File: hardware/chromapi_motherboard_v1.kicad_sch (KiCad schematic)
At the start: 9 parts

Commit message: add spi todo
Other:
- note added: "[todo] correct SPI MISO/MOSI connection mismatch"
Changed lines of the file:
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@@
+		)
+	)
+	(text "[todo] correct SPI MISO/MOSI connection mismatch"
+		(exclude_from_sim no)
+		(at 182.118 57.404 0)
+		(effects
+			(font
+				(size 1.27 1.27)
+			)
+			(justify left bottom)
 		)
 	)

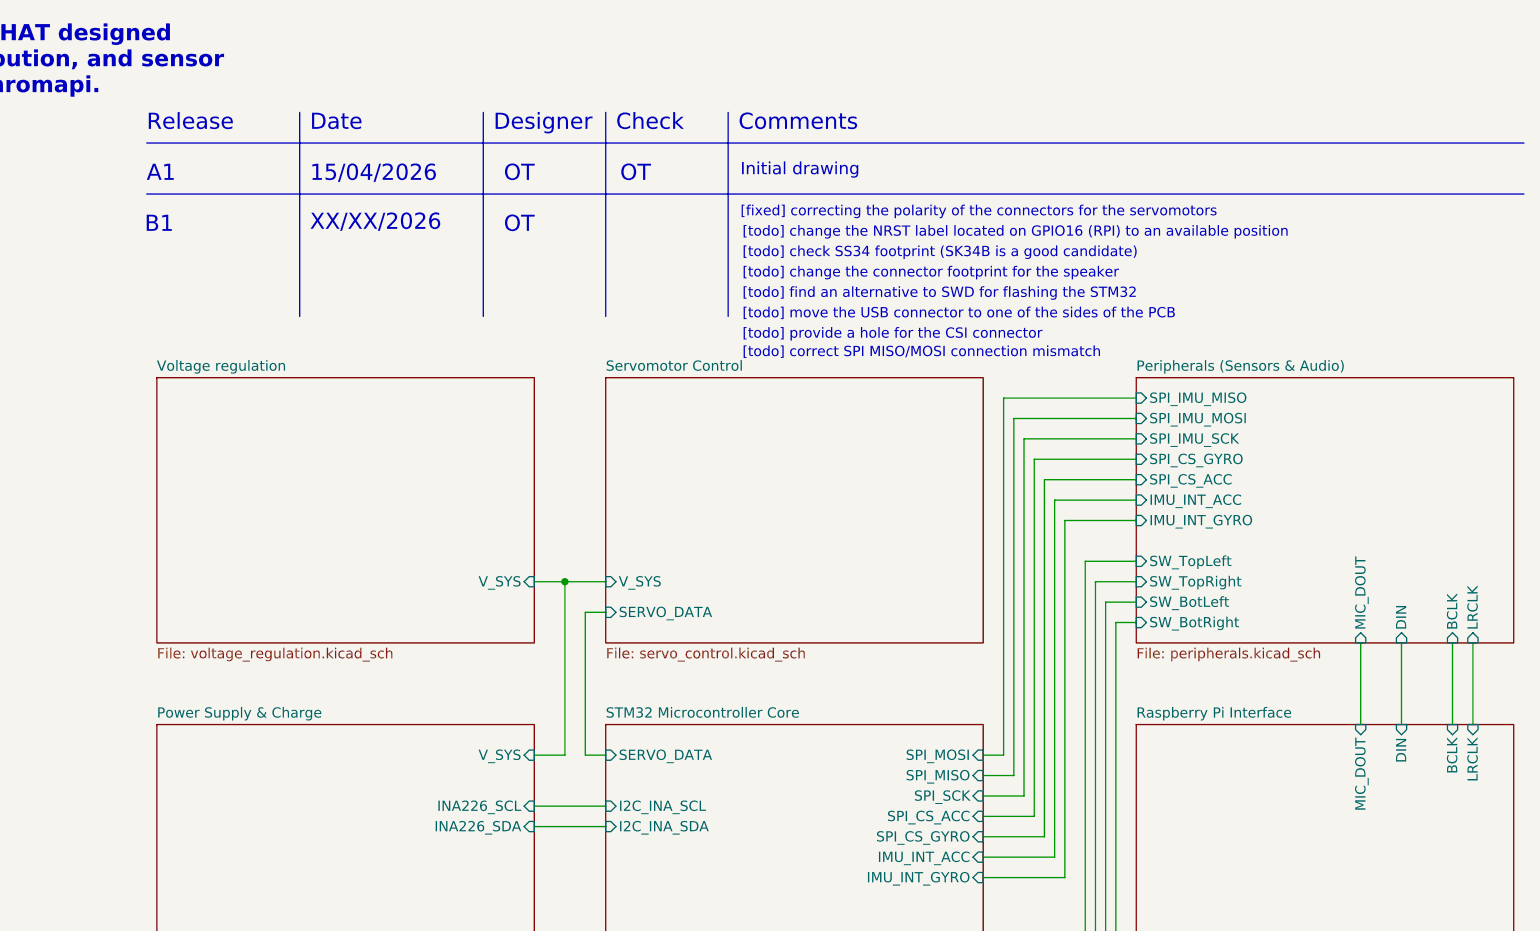
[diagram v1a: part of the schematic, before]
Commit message: fix spi connection mismatch
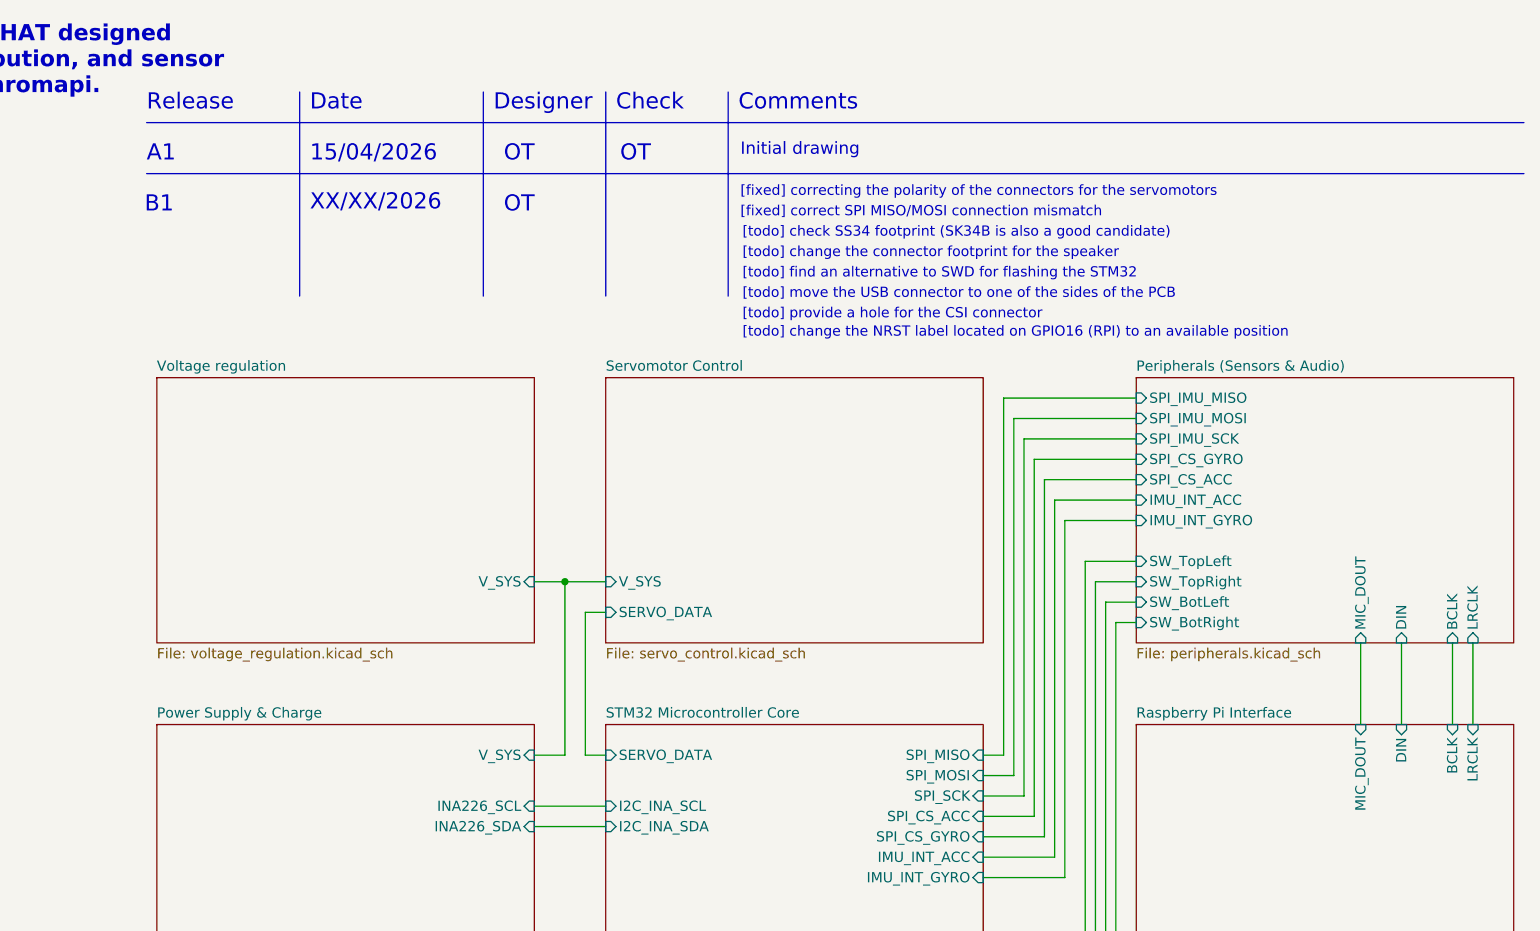
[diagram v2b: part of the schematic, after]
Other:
- note added: "[fixed] correct SPI MISO/MOSI connection mismatch"
- note added: "[todo] check SS34 footprint (SK34B is also a good candidate)"
- note removed: "[todo] check SS34 footprint (SK34B is a good candidate)"
- note removed: "[todo] correct SPI MISO/MOSI connection mismatch"
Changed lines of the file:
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@@
 	(text "[todo] change the connector footprint for the speaker"
 		(exclude_from_sim no)
-		(at 182.118 47.498 0)
+		(at 182.118 44.958 0)
 		(effects
 			(font
@@
 	(text "[todo] change the NRST label located on GPIO16 (RPI) to an available position"
 		(exclude_from_sim no)
-		(at 182.118 42.418 0)
+		(at 182.118 54.864 0)
 		(effects
 			(font
@@
 		)
 	)
-	(text "[todo] check SS34 footprint (SK34B is a good candidate)"
+	(text "[todo] check SS34 footprint (SK34B is also a good candidate)"
 		(exclude_from_sim no)
-		(at 182.118 44.958 0)
+		(at 182.118 42.418 0)
 		(effects
 			(font
@@
 	(text "Check"
 		(exclude_from_sim no)
-		(at 166.37 29.21 0)
+		(at 166.37 26.67 0)
 		(effects
 			(font
@@
 	(text "[fixed] correcting the polarity of the connectors for the servomotors"
 		(exclude_from_sim no)
-		(at 181.864 39.878 0)
+		(at 181.864 37.338 0)
 		(effects
 			(font
@@
 	(text "B1"
 		(exclude_from_sim no)
-		(at 107.696 41.91 0)
+		(at 107.696 39.37 0)
 		(effects
 			(font
@@
 	(text "[todo] provide a hole for the CSI connector "
 		(exclude_from_sim no)
-		(at 182.118 55.118 0)
+		(at 182.118 52.578 0)
 		(effects
 			(font
@@
 	(text "OT"
 		(exclude_from_sim no)
-		(at 166.878 35.56 0)
+		(at 166.878 33.02 0)
 		(effects
 			(font
@@
 	(text "OT"
 		(exclude_from_sim no)
-		(at 152.4 41.91 0)
+		(at 152.4 39.37 0)
 		(effects
 			(font
@@
 	(text "Initial drawing"
 		(exclude_from_sim no)
-		(at 181.864 34.798 0)
+		(at 181.864 32.258 0)
 		(effects
 			(font
@@
 	(text "Release"
 		(exclude_from_sim no)
-		(at 107.95 29.21 0)
+		(at 107.95 26.67 0)
 		(effects
 			(font
@@
 	(text "XX/XX/2026"
 		(exclude_from_sim no)
-		(at 128.27 41.656 0)
+		(at 128.27 39.116 0)
 		(effects
 			(font
@@
 	(text "[todo] move the USB connector to one of the sides of the PCB"
 		(exclude_from_sim no)
-		(at 182.118 52.578 0)
+		(at 182.118 50.038 0)
 		(effects
 			(font
@@
 	(text "[todo] find an alternative to SWD for flashing the STM32"
 		(exclude_from_sim no)
-		(at 182.118 50.038 0)
+		(at 182.118 47.498 0)
 		(effects
 			(font
@@
 	(text "OT"
 		(exclude_from_sim no)
-		(at 152.4 35.56 0)
+		(at 152.4 33.02 0)
 		(effects
 			(font
@@
 	(text "Date"
 		(exclude_from_sim no)
-		(at 128.27 29.21 0)
+		(at 128.27 26.67 0)
 		(effects
 			(font
@@
 	(text "15/04/2026"
 		(exclude_from_sim no)
-		(at 128.27 35.56 0)
+		(at 128.27 33.02 0)
 		(effects
 			(font
@@
 	(text "Comments"
 		(exclude_from_sim no)
-		(at 181.61 29.21 0)
+		(at 181.61 26.67 0)
 		(effects
 			(font
@@
 	(text "A1"
 		(exclude_from_sim no)
-		(at 107.95 35.56 0)
+		(at 107.95 33.02 0)
 		(effects
 			(font
@@
 	(text "Designer"
 		(exclude_from_sim no)
-		(at 151.13 29.21 0)
+		(at 151.13 26.67 0)
 		(effects
 			(font
@@
 		)
 	)
-	(text "[todo] correct SPI MISO/MOSI connection mismatch"
+	(text "[fixed] correct SPI MISO/MOSI connection mismatch"
 		(exclude_from_sim no)
-		(at 182.118 57.404 0)
+		(at 181.864 39.878 0)
 		(effects
 			(font
@@
 	(wire
 		(pts
+			(xy 212.09 106.68) (xy 214.63 106.68)
+		)
+		(stroke
+			(width 0)
+			(type default)
+		)
+	)
+	(wire
+		(pts
 			(xy 156.21 115.57) (xy 165.1 115.57)
 		)
@@
 	(wire
 		(pts
-			(xy 218.44 69.85) (xy 218.44 114.3)
+			(xy 214.63 62.23) (xy 231.14 62.23)
 		)
 		(stroke
@@
 	(wire
 		(pts
-			(xy 214.63 106.68) (xy 214.63 62.23)
+			(xy 218.44 69.85) (xy 218.44 114.3)
 		)
 		(stroke
@@
 	(wire
 		(pts
-			(xy 212.09 106.68) (xy 214.63 106.68)
+			(xy 214.63 106.68) (xy 214.63 62.23)
 		)
 		(stroke
@@
 	(polyline
 		(pts
-			(xy 107.95 36.83) (xy 279.4 36.83)
+			(xy 107.95 34.29) (xy 279.4 34.29)
+		)
+		(stroke
+			(width 0)
+			(type default)
+		)
+	)
+	(wire
+		(pts
+			(xy 215.9 64.77) (xy 231.14 64.77)
 		)
 		(stroke
@@
 	(polyline
 		(pts
-			(xy 127 26.67) (xy 127 52.07)
+			(xy 127 24.13) (xy 127 49.53)
 		)
 		(stroke
@@
 	(polyline
 		(pts
-			(xy 107.95 30.48) (xy 279.4 30.48)
+			(xy 107.95 27.94) (xy 279.4 27.94)
 		)
 		(stroke
@@
 	(polyline
 		(pts
-			(xy 149.86 26.67) (xy 149.86 52.07)
-		)
-		(stroke
-			(width 0)
-			(type default)
-		)
-	)
-	(wire
-		(pts
-			(xy 215.9 64.77) (xy 231.14 64.77)
+			(xy 149.86 24.13) (xy 149.86 49.53)
 		)
 		(stroke
@@
 	(polyline
 		(pts
-			(xy 165.1 26.67) (xy 165.1 52.07)
+			(xy 165.1 24.13) (xy 165.1 49.53)
 		)
 		(stroke
@@
 	(polyline
 		(pts
-			(xy 180.34 26.67) (xy 180.34 52.07)
+			(xy 180.34 24.13) (xy 180.34 49.53)
 		)
 		(stroke
@@
 	(wire
 		(pts
-			(xy 212.09 146.05) (xy 231.14 146.05)
+			(xy 212.09 109.22) (xy 215.9 109.22)
 		)
 		(stroke
@@
 	(wire
 		(pts
-			(xy 214.63 62.23) (xy 231.14 62.23)
+			(xy 212.09 146.05) (xy 231.14 146.05)
 		)
 		(stroke
@@
 	(wire
 		(pts
-			(xy 212.09 109.22) (xy 215.9 109.22)
-		)
-		(stroke
-			(width 0)
-			(type default)
-		)
-	)
-	(wire
-		(pts
 			(xy 222.25 121.92) (xy 222.25 77.47)
 		)
@@
 		)
 		(pin "SPI_MOSI" input
-			(at 212.09 106.68 0)
+			(at 212.09 109.22 0)
 			(effects
 				(font
@@
 		)
 		(pin "SPI_MISO" input
-			(at 212.09 109.22 0)
+			(at 212.09 106.68 0)
 			(effects
 				(font

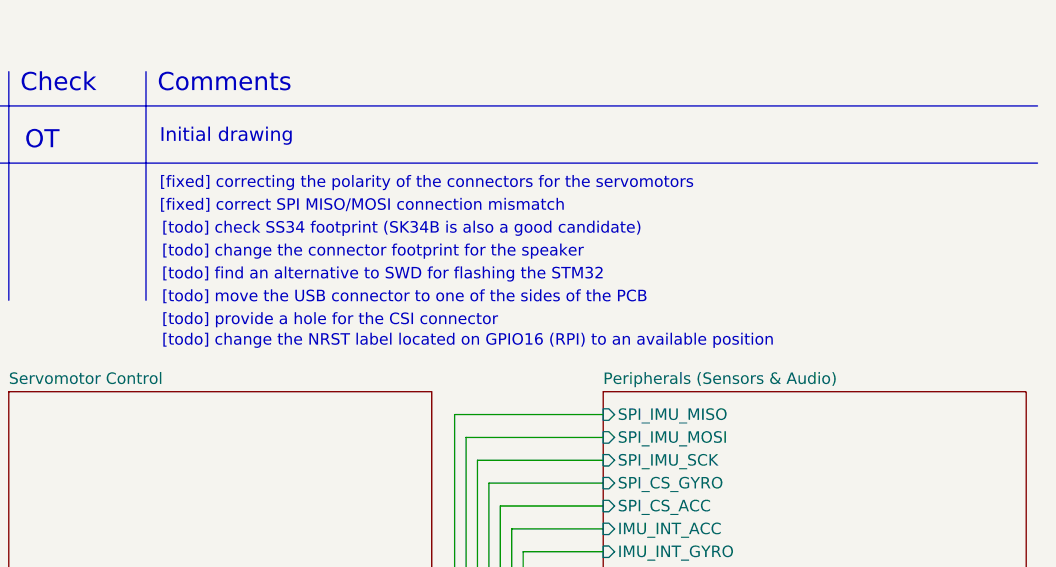
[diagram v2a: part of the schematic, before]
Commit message: [fixed] change the connector footprint for the speaker
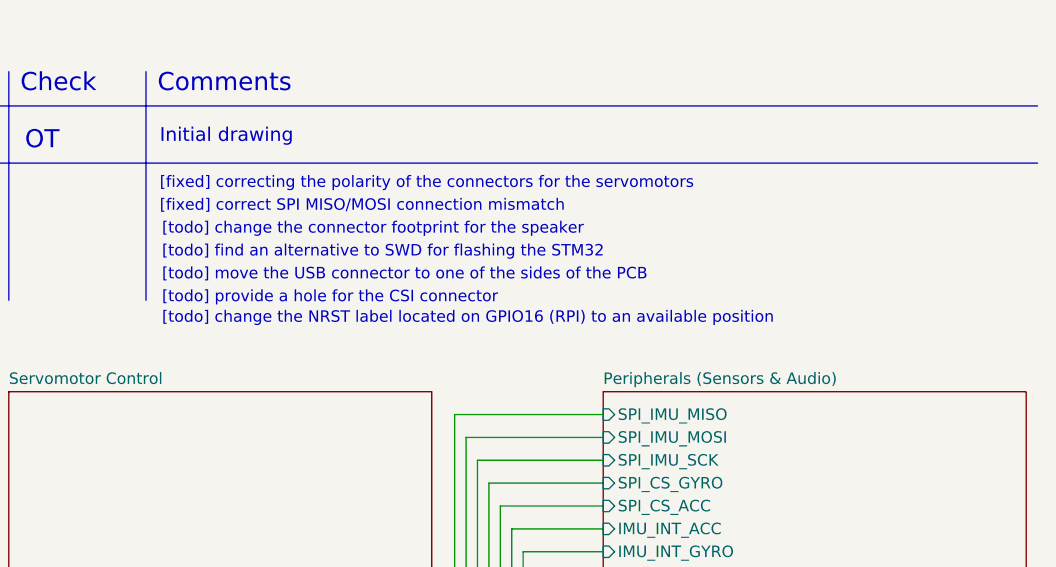
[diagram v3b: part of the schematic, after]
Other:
- note removed: "[todo] check SS34 footprint (SK34B is also a good candidate)"
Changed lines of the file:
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@@
 	(text "[todo] change the connector footprint for the speaker"
 		(exclude_from_sim no)
-		(at 182.118 44.958 0)
+		(at 182.118 42.418 0)
 		(effects
 			(font
@@
 	(text "[todo] change the NRST label located on GPIO16 (RPI) to an available position"
 		(exclude_from_sim no)
-		(at 182.118 54.864 0)
-		(effects
-			(font
-				(size 1.27 1.27)
-			)
-			(justify left bottom)
-		)
-	)
-	(text "[todo] check SS34 footprint (SK34B is also a good candidate)"
-		(exclude_from_sim no)
-		(at 182.118 42.418 0)
+		(at 182.118 52.324 0)
 		(effects
 			(font
@@
 	(text "[todo] provide a hole for the CSI connector "
 		(exclude_from_sim no)
-		(at 182.118 52.578 0)
+		(at 182.118 50.038 0)
 		(effects
 			(font
@@
 	(text "[todo] move the USB connector to one of the sides of the PCB"
 		(exclude_from_sim no)
-		(at 182.118 50.038 0)
+		(at 182.118 47.498 0)
 		(effects
 			(font
@@
 	(text "[todo] find an alternative to SWD for flashing the STM32"
 		(exclude_from_sim no)
-		(at 182.118 47.498 0)
+		(at 182.118 44.958 0)
 		(effects
 			(font

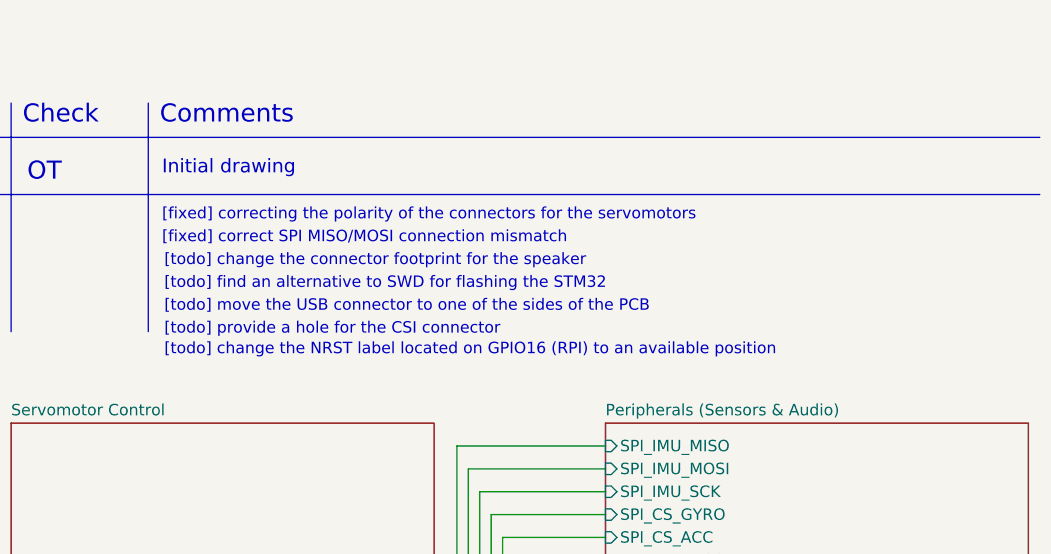
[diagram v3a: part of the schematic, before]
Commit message: [fix] change the connector footprint for the speaker
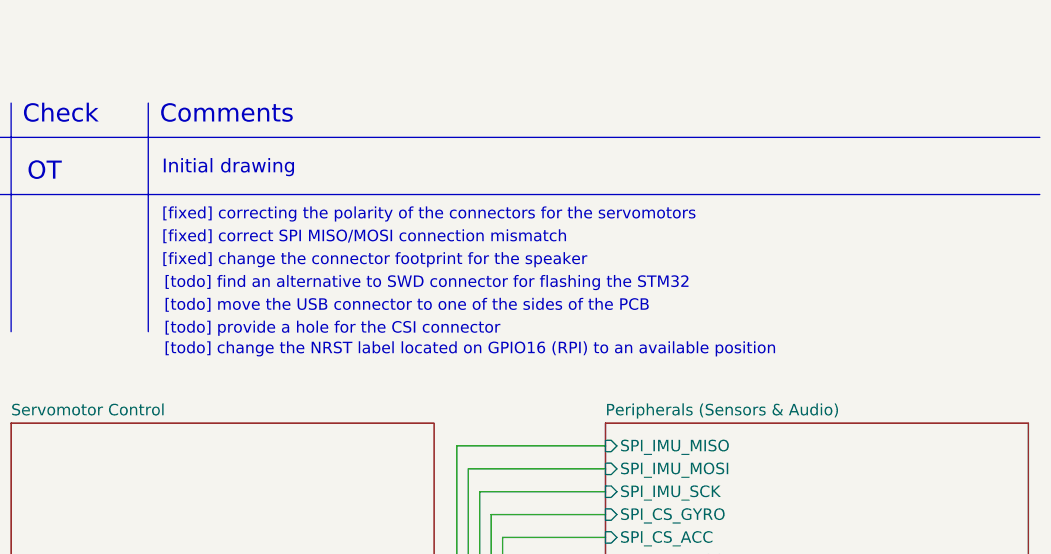
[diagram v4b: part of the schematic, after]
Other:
- note added: "[fixed] change the connector footprint for the speaker"
- note added: "[todo] find an alternative to SWD connector for flashing the STM32"
- note removed: "[todo] change the connector footprint for the speaker"
- note removed: "[todo] find an alternative to SWD for flashing the STM32"
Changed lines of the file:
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@@
 		(comment 1 "Ousmane THIONGANE")
 	)
-	(text "[todo] change the connector footprint for the speaker"
+	(text "[fixed] change the connector footprint for the speaker"
 		(exclude_from_sim no)
-		(at 182.118 42.418 0)
+		(at 181.864 42.418 0)
 		(effects
 			(font
@@
 		)
 	)
-	(text "[todo] find an alternative to SWD for flashing the STM32"
+	(text "[todo] find an alternative to SWD connector for flashing the STM32"
 		(exclude_from_sim no)
 		(at 182.118 44.958 0)
